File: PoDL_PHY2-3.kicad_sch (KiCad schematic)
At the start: 45 parts, among them Q13 DMG3414U, Q14 MMBTA06, Q15 MMBT3904, Q16 DMG3414U, Q17 DMG3414U, Q18 MMBT3904, Q19 DMG3414U, Q20 MMBTA06, Q21 MMBT3904, Q22 DMG3414U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

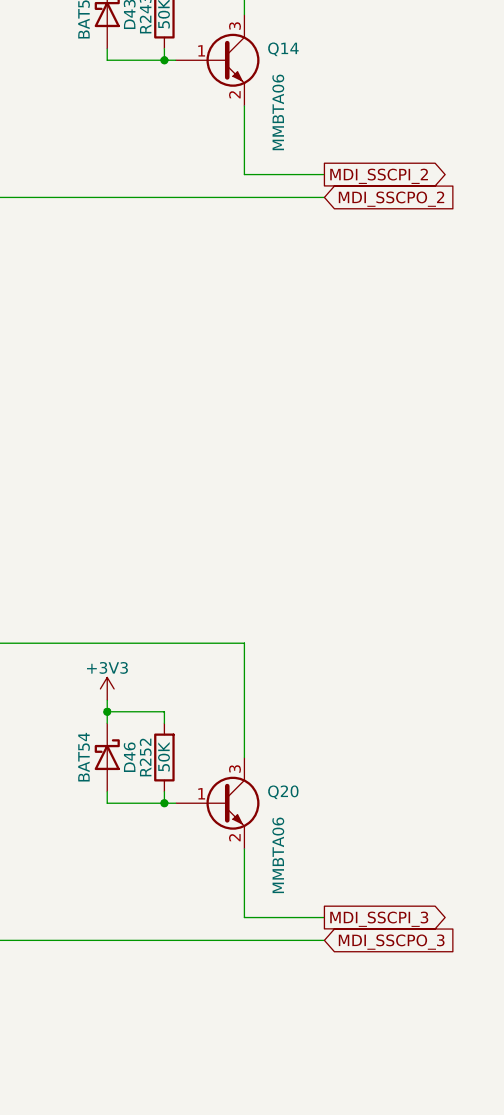
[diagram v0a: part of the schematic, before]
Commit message: Correcting SCCP spelling
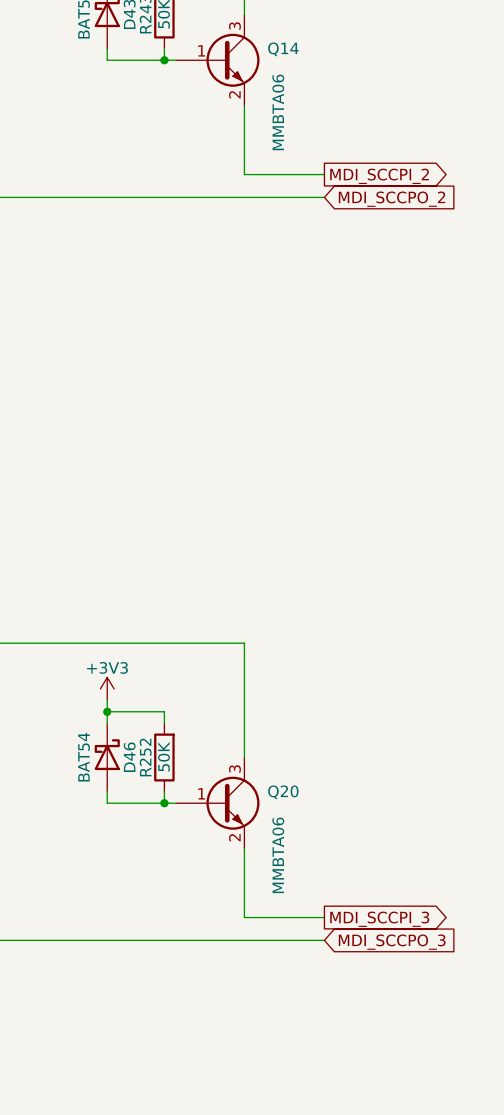
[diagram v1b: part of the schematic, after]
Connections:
- net MDI_SSCPI_2 renamed MDI_SCCPI_2
- net MDI_SSCPI_3 renamed MDI_SCCPI_3
- net MDI_SSCPO_2 renamed MDI_SCCPO_2
- net MDI_SSCPO_3 renamed MDI_SCCPO_3
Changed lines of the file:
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@@
     (effects (font (size 2 2) (thickness 0.254) bold) (justify left bottom))
   )
-  (global_label "MDI_SSCPO_2" (shape input) (at 198.12 60.96 0) (fields_autoplaced)
+  (global_label "MDI_SCCPO_2" (shape input) (at 198.12 60.96 0) (fields_autoplaced)
     (effects (font (size 1.27 1.27)) (justify left))
     (property "Intersheet References" "${INTERSHEET_REFS}" (id 0) (at 213.2936 60.8806 0)
@@
     )
   )
-  (global_label "MDI_SSCPI_3" (shape output) (at 198.12 140.97 0) (fields_autoplaced)
+  (global_label "MDI_SCCPI_3" (shape output) (at 198.12 140.97 0) (fields_autoplaced)
     (effects (font (size 1.27 1.27)) (justify left))
     (property "Intersheet References" "${INTERSHEET_REFS}" (id 0) (at 212.5679 140.8906 0)
@@
     )
   )
-  (global_label "MDI_SSCPO_3" (shape input) (at 198.12 143.51 0) (fields_autoplaced)
+  (global_label "MDI_SCCPO_3" (shape input) (at 198.12 143.51 0) (fields_autoplaced)
     (effects (font (size 1.27 1.27)) (justify left))
     (property "Intersheet References" "${INTERSHEET_REFS}" (id 0) (at 213.2936 143.4306 0)
@@
     )
   )
-  (global_label "MDI_SSCPI_2" (shape output) (at 198.12 58.42 0) (fields_autoplaced)
+  (global_label "MDI_SCCPI_2" (shape output) (at 198.12 58.42 0) (fields_autoplaced)
     (effects (font (size 1.27 1.27)) (justify left))
     (property "Intersheet References" "${INTERSHEET_REFS}" (id 0) (at 212.5679 58.3406 0)
